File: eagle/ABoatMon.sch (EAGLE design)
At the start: 33 parts, among them J1 VUSB, J2 GND, J3 GND, J4 LIPO, J5 U.FL, X1 MKDSN1,5/2-5,08

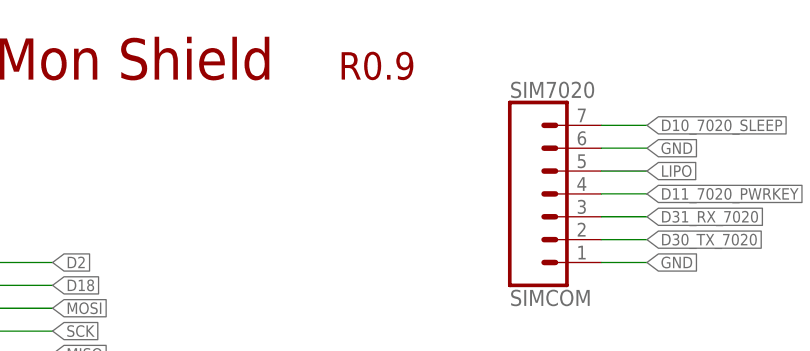
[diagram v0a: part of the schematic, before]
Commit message: Moved JSTs
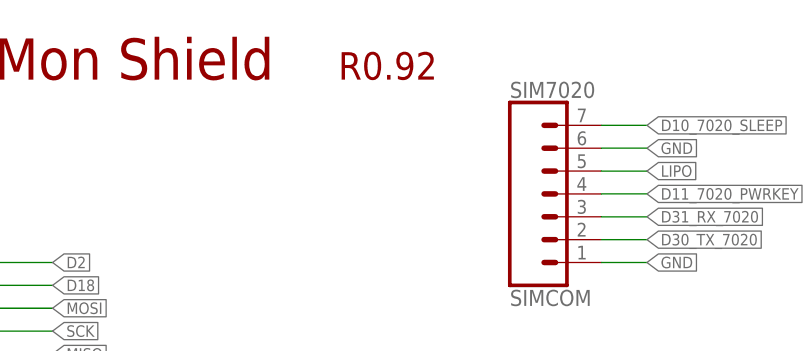
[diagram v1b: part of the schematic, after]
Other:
- note added: "R0.92"
- note removed: "R0.9"
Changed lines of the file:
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@@
 <attributes>
 <attribute name="CNAME" value="MoteinoMega ABoatMon Shield"/>
-<attribute name="CREVISION" value="0.9"/>
+<attribute name="CREVISION" value="0.92"/>
 <attribute name="DESIGNER" value="gregcope@gmail.com"/>
 </attributes>
@@
 Max 600mA 96% eff</text>
 <text x="101.6" y="162.56" size="3.048" layer="94" ratio="12">Greg Cope</text>
-<text x="189.23" y="167.64" size="3.048" layer="94" ratio="12">R0.9</text>
+<text x="189.23" y="167.64" size="3.048" layer="94" ratio="12">R0.92</text>
 <text x="101.6" y="167.64" size="4.572" layer="94" ratio="15">MoteinoM0 AboatMon Shield</text>
 <text x="187.96" y="25.4" size="1.27" layer="91">Consider MCP1810 lower shutdown current 1na</text>

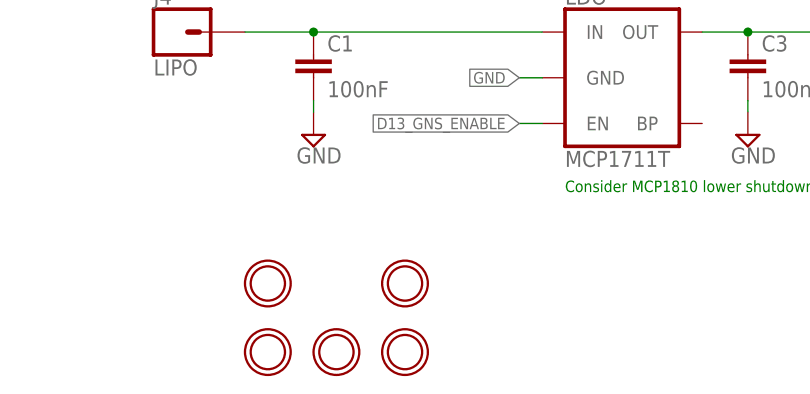
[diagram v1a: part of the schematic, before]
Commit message: Moved SIM7000 up a bit
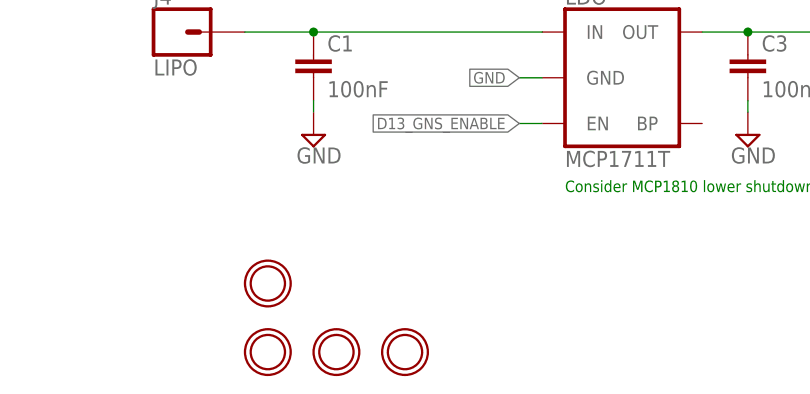
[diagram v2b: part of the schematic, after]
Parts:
- removed U$1: MOUNTINGHOLE2.5, microbuilder:MOUNTINGHOLE2.5
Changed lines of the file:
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@@
 <part name="J3" library="SparkFun-Connectors" deviceset="CONN_01" device="" value="GND"/>
 <part name="VCC" library="microbuilder" deviceset="HEADER-1X2" device="ROUND" value="JUMPER"/>
-<part name="U$1" library="microbuilder" deviceset="MOUNTINGHOLE" device="2.5"/>
 <part name="GND" library="microbuilder" deviceset="MOUNTINGHOLE" device="2.5"/>
 <part name="U$7" library="microbuilder" deviceset="MOUNTINGHOLE" device="2.5"/>
@@
 <attribute name="VALUE" x="189.23" y="83.82" size="1.778" layer="96"/>
 </instance>
-<instance part="U$1" gate="G$1" x="170.18" y="15.24" smashed="yes"/>
 <instance part="GND" gate="G$1" x="162.56" y="7.62" smashed="yes"/>
 <instance part="U$7" gate="G$1" x="170.18" y="7.62" smashed="yes"/>
